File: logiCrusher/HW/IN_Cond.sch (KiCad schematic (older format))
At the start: 5 parts

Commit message: Added the front plate files
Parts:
- removed J?: Barrel_Jack_Switch, Eurocad:PJ301M-12, symbol Connector:Barrel_Jack_Switch
- removed Q?: MMBT3904, Package_TO_SOT_SMD:SOT-23, symbol Transistor_BJT:MMBT3904
- removed R?: 10k, Resistor_SMD:R_0805_2012Metric, symbol Device:R_US
- added C? (x4): 1uF, Capacitor_SMD:C_0805_2012Metric, symbol Device:C_Small
- added D? (x2): D, symbol Device:D
- added R? (x7): 1M, Resistor_SMD:R_0805_2012Metric, symbol Device:R_US
- added R?: 10R, Resistor_SMD:R_0805_2012Metric, symbol Device:R_US
- added U1, U2 (x2): LM2904DR, Package_SO:SOIC-8_3.9x4.9mm_P1.27mm, symbol Device:Opamp_Dual_Generic
- R?: value 100k -> 10k
- R?: value 1M -> 20k
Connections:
- net labels added: +1.65V, +12V, -12V, Vin, Vout
- net labels removed: TRIG
- wire segments 11 -> 65
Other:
- note added: "1.65V Reference"
- moved on the sheet: R?

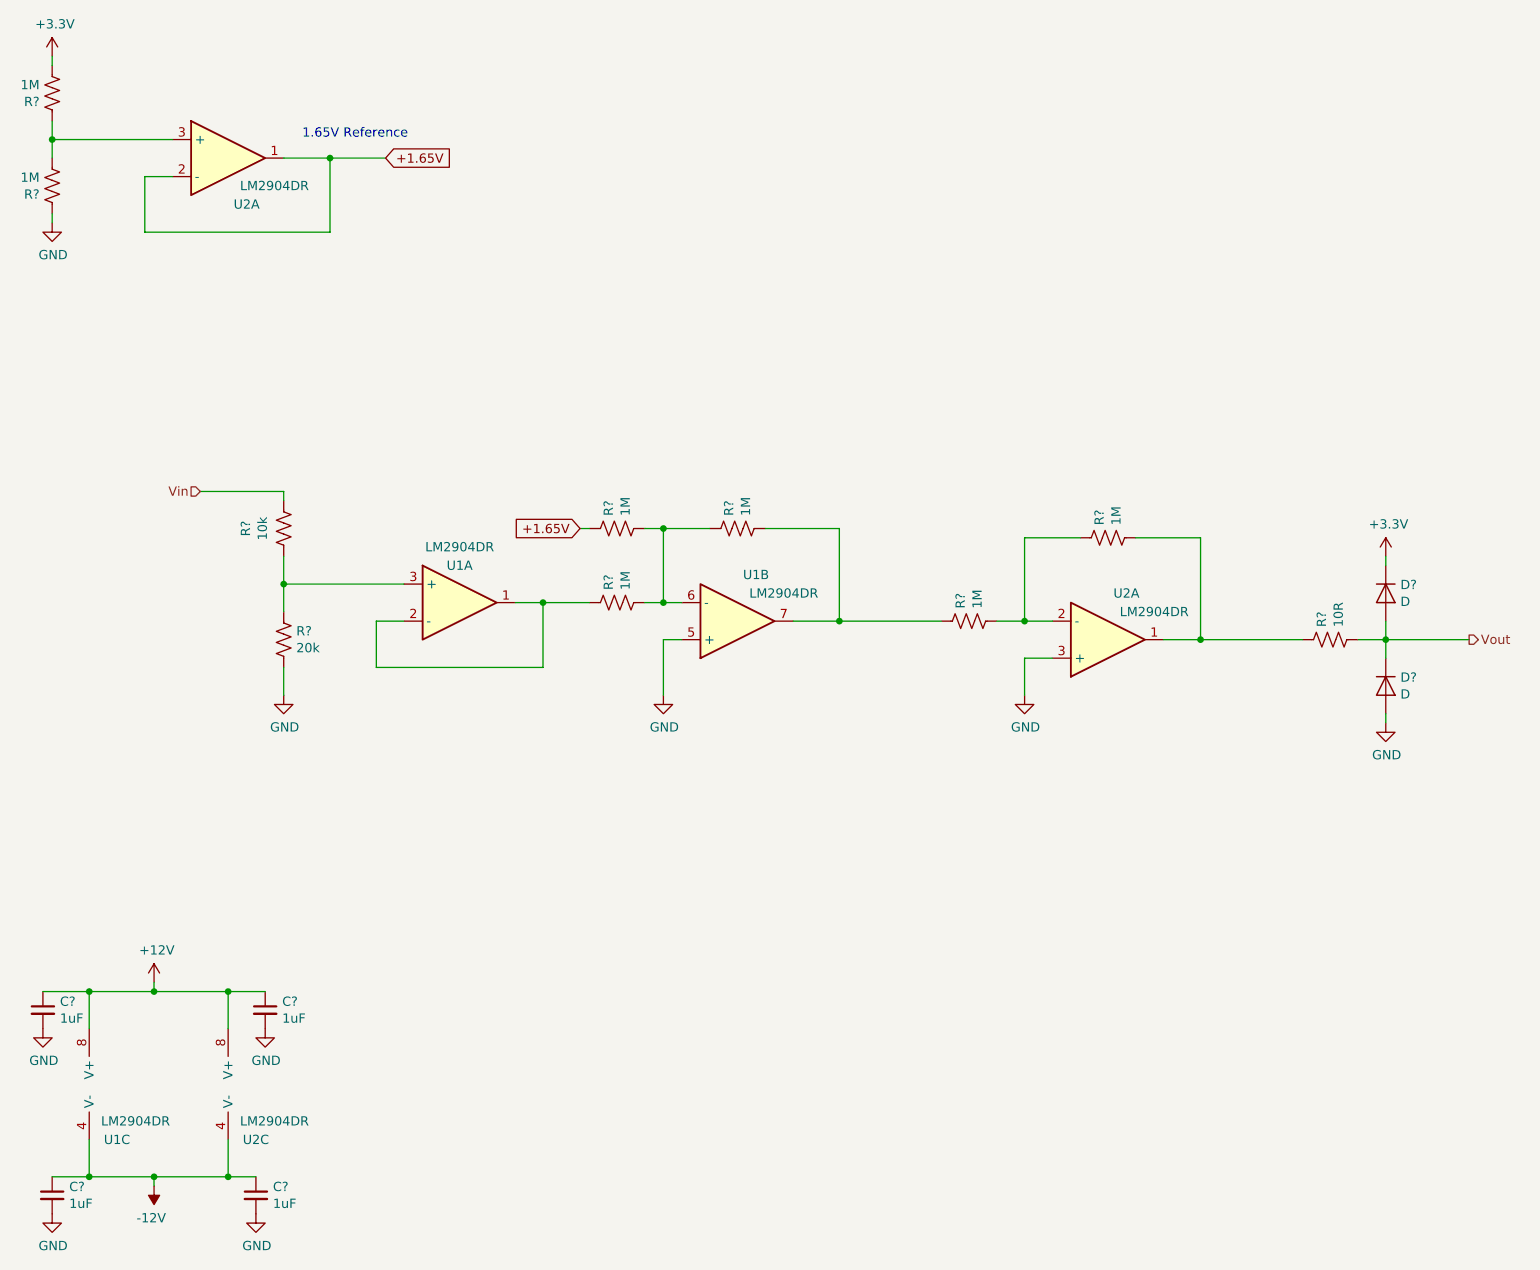
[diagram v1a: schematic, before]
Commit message: Worked on the HW for the mcu module
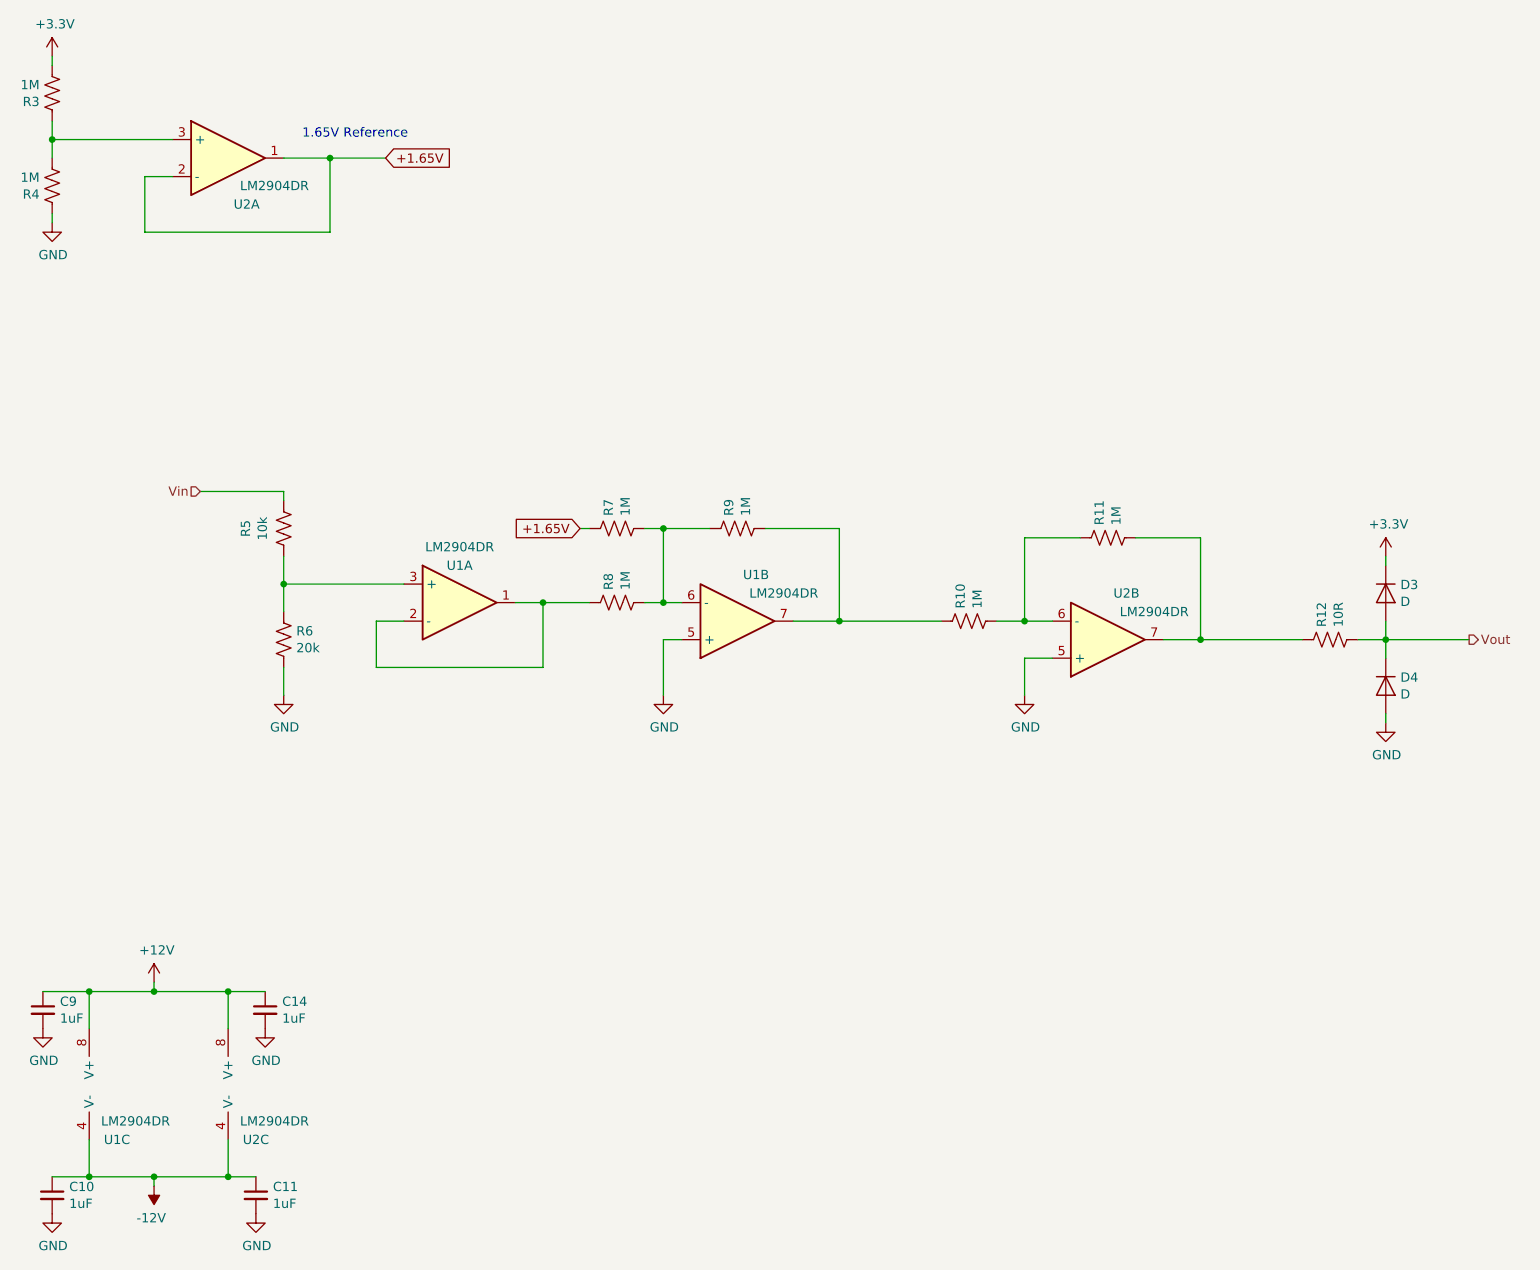
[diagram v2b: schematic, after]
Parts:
- gave numbers to parts that had none: 16
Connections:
- net GND: now also U2.5 (+); no longer U2.3 (+)
- net at R11.1, R12.2: now also U2.7; no longer U2.1
- net at R10.1, R11.2: now also U2.6 (-); no longer U2.2 (-)

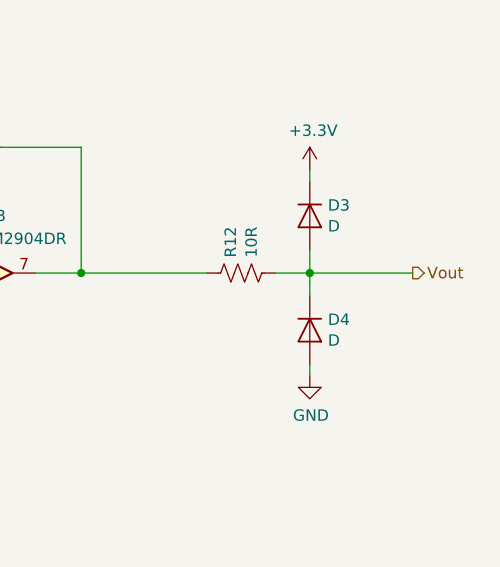
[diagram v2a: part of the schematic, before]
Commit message: Worked on the layout for the logicrusher
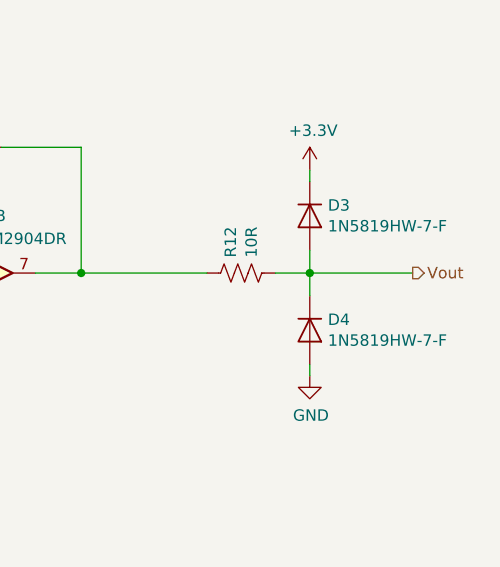
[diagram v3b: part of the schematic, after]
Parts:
- D3, D4: value D -> 1N5819HW-7-F; footprint (none) -> Diode_SMD:D_SOD-123
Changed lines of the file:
@@
 P 8250 3900
 F 0 "D3" V 8204 3979 50  0000 L CNN
-F 1 "D" V 8295 3979 50  0000 L CNN
-F 2 "" H 8250 3900 50  0001 C CNN
+F 1 "1N5819HW-7-F" V 8295 3979 50  0000 L CNN
+F 2 "Diode_SMD:D_SOD-123" H 8250 3900 50  0001 C CNN
 F 3 "~" H 8250 3900 50  0001 C CNN
 	1    8250 3900
@@
 P 8250 4400
 F 0 "D4" V 8204 4479 50  0000 L CNN
-F 1 "D" V 8295 4479 50  0000 L CNN
-F 2 "" H 8250 4400 50  0001 C CNN
+F 1 "1N5819HW-7-F" V 8295 4479 50  0000 L CNN
+F 2 "Diode_SMD:D_SOD-123" H 8250 4400 50  0001 C CNN
 F 3 "~" H 8250 4400 50  0001 C CNN
 	1    8250 4400

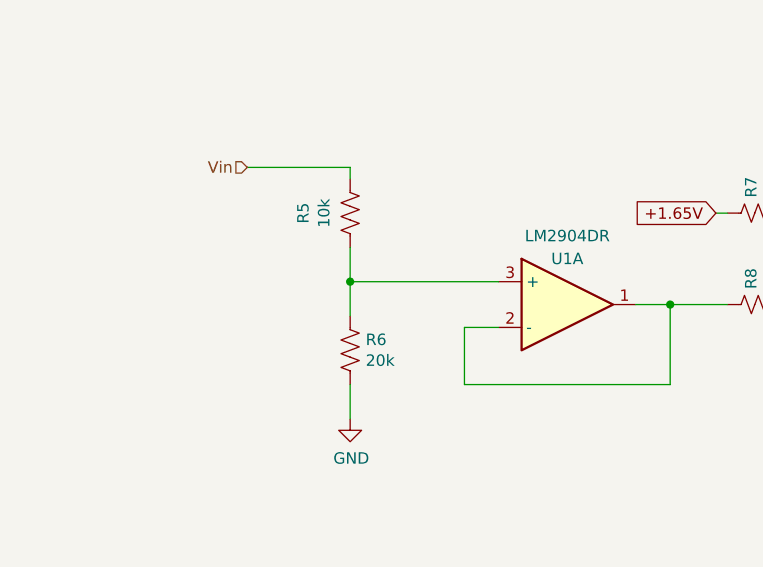
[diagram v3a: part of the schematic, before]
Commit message: Added simulation files and fixed the values of the gain resistors.
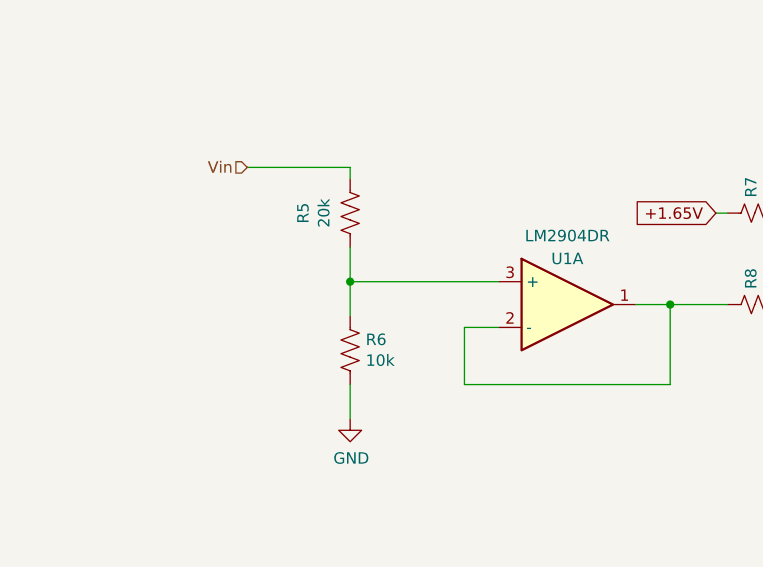
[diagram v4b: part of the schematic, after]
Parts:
- R5: value 10k -> 20k
- R6: value 20k -> 10k
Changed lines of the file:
@@
 P 2300 3550
 F 0 "R5" V 2095 3550 50  0000 C CNN
-F 1 "10k" V 2186 3550 50  0000 C CNN
+F 1 "20k" V 2186 3550 50  0000 C CNN
 F 2 "Resistor_SMD:R_0805_2012Metric" V 2340 3540 50  0001 C CNN
 F 3 "~" H 2300 3550 50  0001 C CNN
@@
 P 2300 4150
 F 0 "R6" H 2232 4104 50  0000 R CNN
-F 1 "20k" H 2232 4195 50  0000 R CNN
+F 1 "10k" H 2232 4195 50  0000 R CNN
 F 2 "Resistor_SMD:R_0805_2012Metric" V 2340 4140 50  0001 C CNN
 F 3 "~" H 2300 4150 50  0001 C CNN
